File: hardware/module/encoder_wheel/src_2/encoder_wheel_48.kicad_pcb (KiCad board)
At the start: 2 copper layers, 74 x 74 mm, 2 parts

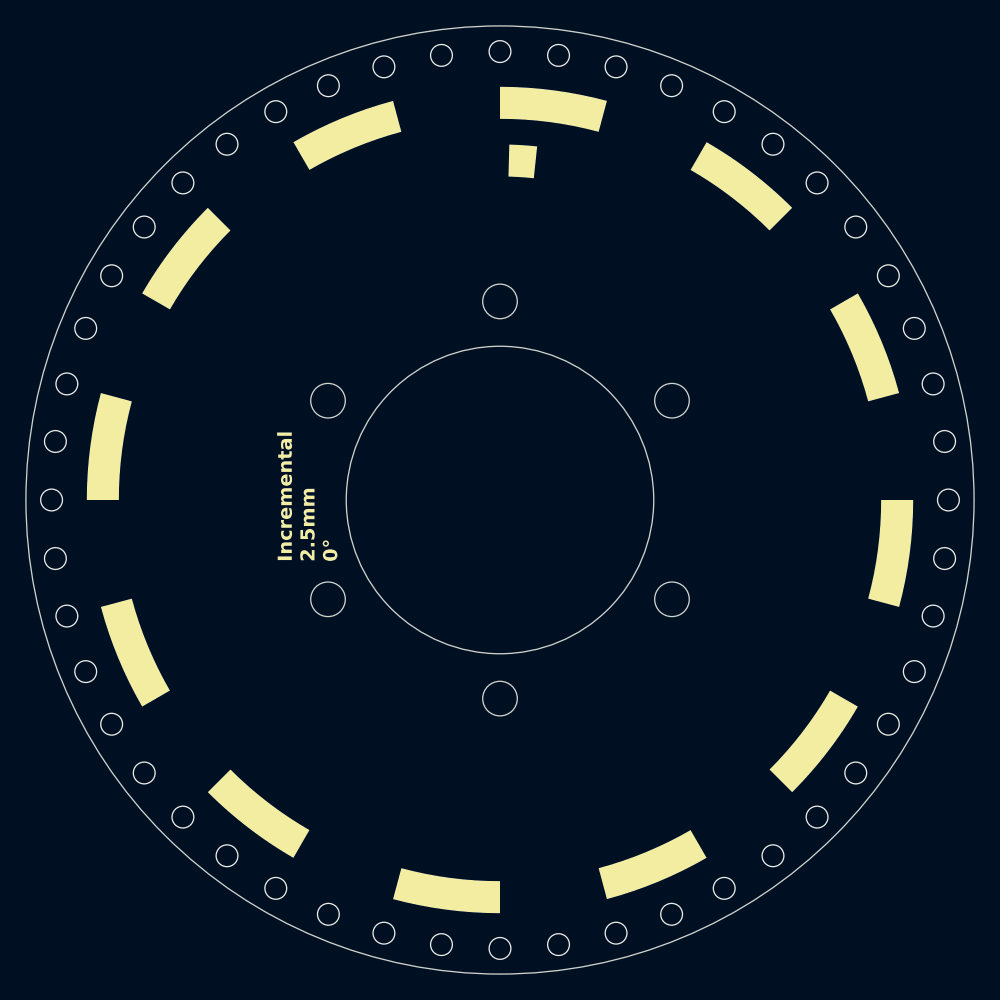
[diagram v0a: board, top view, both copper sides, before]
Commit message: Change from absolute encoder to incremental encoder.
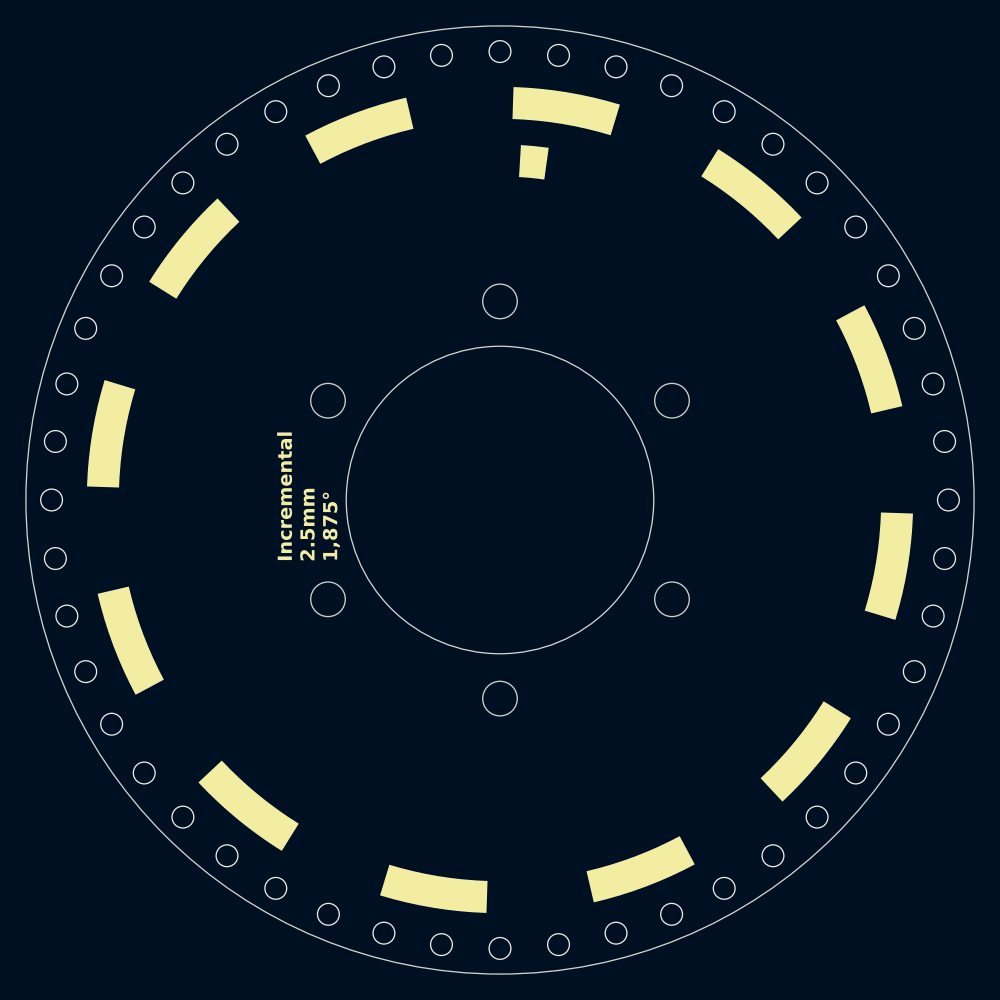
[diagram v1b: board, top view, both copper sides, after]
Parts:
- turned REF** to -1.875 degrees
- turned REF** to 178.125 degrees
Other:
- board text added: "Incremental 2.5mm 1,875°"
- board text added: "Incremental 2.5mm 5.625°"
- board text removed: "Incremental 2.5mm 0°"
- board text removed: "Incremental 2.5mm 3.75°"
